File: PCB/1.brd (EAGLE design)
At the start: 127 x 92.4 mm, 52 parts, among them IC1 7805, IC2 MEGA32-P, T1 2N2219, T2 2N2219, T3 2N2219, T4 2N2219, T5 BC337, T6 BC337, T7 BC337, X1 9v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

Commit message: Fix PCB
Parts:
- moved R1 49.7 mm to (114.3, 17.8)
- moved LED1 47.0 mm to (119.4, 10.2), turned to 270 degrees
- moved X2 46.0 mm to (108.0, 11.4)
- moved C2 45.7 mm to (86.4, 19.1)
- moved D1 39.6 mm to (92.7, 12.7)
- moved IC1 35.7 mm to (81.3, 10.2)
- moved C1 33.1 mm to (62.2, 10.2)
- moved B1 31.9 mm to (50.8, 10.2)
- moved X1 30.5 mm to (38.1, 7.62), turned to 180 degrees
- moved D4 29.5 mm to (108.0, 57.1)
- moved T5 28.2 mm to (96.5, 57.1), turned to 270 degrees
- moved R17 25.9 mm to (102.9, 74.9)
- moved D5 25.9 mm to (102.9, 61.0)
- moved T6 25.7 mm to (96.5, 63.5), turned to 270 degrees
- moved R16 25.7 mm to (108.0, 69.8)
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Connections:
- net N$44: now also X2.1; no longer X2.2
- net SW1: now also X6.1; no longer X6.2
- net VCC: now also X2.2, X6.2; no longer X2.1, X6.1
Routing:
- net GND: track 373.2 -> 598.2 mm, vias 5 -> 2
- net SW2: track 89.7 -> 27.5 mm, vias 2 -> 0
- net VCC: track 222.6 -> 184.6 mm
- net N$28: track 36.3 -> 73.4 mm, vias 2 -> 0
- net N$35: track 31.4 -> 14.2 mm
- net N$44: track 43.4 -> 59.4 mm
- net N$40: track 30.1 -> 14.1 mm
- net N$39: track 45.1 -> 58.5 mm
- net N$37: track 9.09 -> 21.5 mm
- net N$42: track 26.4 -> 14.1 mm
- net INT1: track 42.1 -> 33.0 mm
- net SW1: track 35.6 -> 26.7 mm
- net N$26: track 15.2 -> 7.62 mm
- net INT2: track 54.9 -> 47.5 mm, vias 0 -> 2
- net N$43: track 11.7 -> 18.9 mm
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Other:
- board text removed: "0"
- board text removed: "1"
- board text removed: "2"
- board text removed: "A"
- board text removed: "B"
- board text removed: "C"
- board text removed: "D"
- board text removed: "G"
- board text removed: "V"

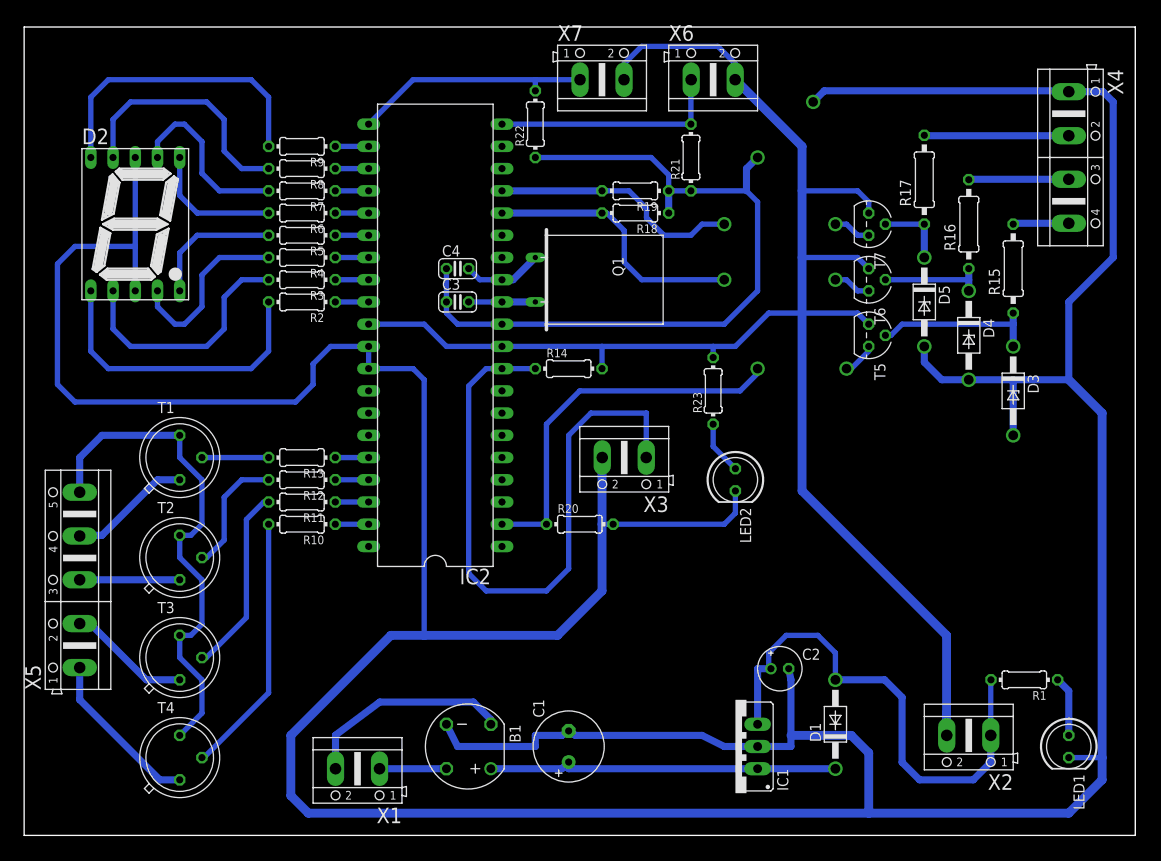
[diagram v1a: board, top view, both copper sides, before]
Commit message: Fix PCB (PCB is working)
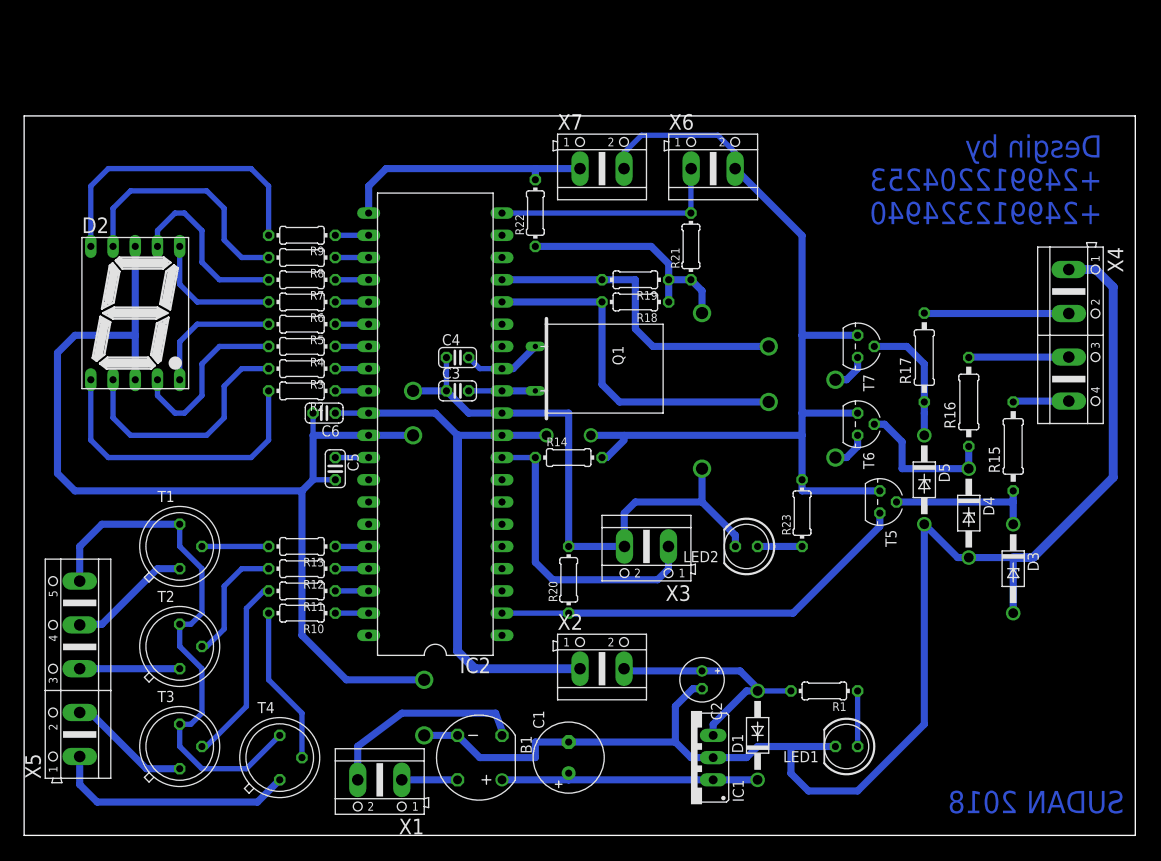
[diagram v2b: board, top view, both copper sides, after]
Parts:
- added C5, C6: 100n, rcl:C025-024X044
- Q1: value (none) -> 16MHz
- moved X2 42.6 mm to (66.0, 19.1), turned to 0 degrees
- moved LED1 25.4 mm to (94.0, 10.2), turned to 180 degrees
- moved R1 22.9 mm to (91.4, 16.5)
- moved R17 20.3 mm to (102.9, 54.6)
- moved D4 20.3 mm to (108.0, 36.8)
- moved D5 20.3 mm to (102.9, 40.6)
- moved X4 20.3 mm to (119.4, 57.1)
- moved D3 20.3 mm to (113.0, 30.5)
- moved R15 20.3 mm to (113.0, 44.5)
- moved R16 20.3 mm to (108.0, 49.5)
- moved T5 19.1 mm to (97.8, 38.1)
- moved R23 17.3 mm to (88.9, 36.8)
- moved T6 16.6 mm to (95.2, 47.0)
- moved T7 14.0 mm to (95.2, 55.9)
- moved T4 11.4 mm to (29.2, 8.89)
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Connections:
- new net N$45: C5.1, IC2.32
- net GND: now also C5.2, C6.2; no longer IC2.32
- net N$44: now also X2.2; no longer X2.1
- net VCC: now also C6.1, X2.1; no longer X2.2
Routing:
- net GND: track 598.2 -> 384.0 mm, vias 2 -> 3
- net N$28: track 73.4 -> 34.9 mm
- net N$44: track 59.4 -> 28.4 mm
- net VCC: track 184.6 -> 172.3 mm, vias 0 -> 1
- net N$38: track 30.0 -> 18.1 mm
- net N$3: track 40.4 -> 30.0 mm
- net INT0: track 35.0 -> 45.1 mm
- net N$43: track 18.9 -> 27.9 mm
- net INT1: track 33.0 -> 41.3 mm
- net N$31: track 8.25 -> 14.7 mm
- net N$30: track 12.1 -> 17.2 mm
- net N$45: track 0.00 -> 3.81 mm
- net N$39: track 58.5 -> 61.6 mm
- net SW2: track 27.5 -> 29.3 mm
- net N$29: track 18.9 -> 17.1 mm
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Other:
- board size 127 x 92.4 mm -> 127 x 82.2 mm
- board text added: "+249912204253"
- board text added: "+249912324940"
- board text added: "Desgin by"
- board text added: "SUDAN 2018"

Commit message: Edit timer and PCB
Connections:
- net INT2: now also IC2.3; no longer IC2.2
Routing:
- net INT2: track 48.8 -> 49.9 mm
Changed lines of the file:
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@@
 </signal>
 <signal name="INT2">
-<contactref element="IC2" pad="2"/>
 <contactref element="R20" pad="1"/>
 <contactref element="T5" pad="1"/>
-<wire x1="54.61" y1="25.4" x2="62.23" y2="25.4" width="0.6096" layer="16"/>
 <wire x1="97.79" y1="36.83" x2="97.79" y2="35.319015625" width="0.8128" layer="16"/>
 <wire x1="97.79" y1="35.319015625" x2="87.870984375" y2="25.4" width="0.8128" layer="16"/>
 <wire x1="87.870984375" y1="25.4" x2="62.23" y2="25.4" width="0.8128" layer="16"/>
+<contactref element="IC2" pad="3"/>
+<wire x1="62.23" y1="25.4" x2="59.69" y2="25.4" width="0.8128" layer="16"/>
+<wire x1="59.69" y1="25.4" x2="57.15" y2="27.94" width="0.8128" layer="16"/>
+<wire x1="57.15" y1="27.94" x2="54.61" y2="27.94" width="0.8128" layer="16"/>
 </signal>
 <signal name="SW2">
